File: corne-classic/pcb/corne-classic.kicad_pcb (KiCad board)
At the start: 2 copper layers, 133.8 x 92.2 mm, 98 parts, among them J1 MJ-4PP-9, J2 OLED, J3 LED, P1 i2c-pin, P2 i2c-pin, SW1 SW_PUSH, SW10 SW_PUSH, SW11 SW_PUSH, SW12 SW_PUSH, SW13 SW_PUSH, SW14 SW_PUSH, SW15 SW_PUSH, SW16 SW_PUSH, SW17 SW_PUSH, SW18 SW_PUSH, SW19 SW_PUSH, SW2 SW_PUSH, SW20 SW_PUSH, SW21 SW_PUSH, SW3 SW_PUSH, SW4 SW_PUSH, SW5 SW_PUSH, SW6 SW_PUSH, SW7 SW_PUSH, SW8 SW_PUSH, SW9 SW_PUSH, U1 ProMicro

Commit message: new stuff
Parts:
- removed the ? at (177.8, 115.8)
- removed the ? at (192.2, 124.2)
- removed the ? at (79.5, 86.8)
- removed the ? at (98.5, 86.8)
- removed the ? at (98.5, 105.8)
- removed the ? at (155.5, 83.0)
- removed the ? at (122.8, 122.8)
- removed G*** (x2): LOGO, kbd:corne
- added ?: , kbd:LEGO_HOLE2, F.Cu at (192.2, 124.2)
- added ?: , kbd:LEGO_HOLE, F.Cu at (155.5, 64.0)
- added ?: , kbd:LEGO_HOLE, F.Cu at (103.8, 122.8)
- added ?: , kbd:LEGO_HOLE, F.Cu at (155.5, 101.8)
- added ?: , kbd:LEGO_HOLE, F.Cu at (117.5, 62.0)
- added ?: , kbd:LEGO_HOLE, F.Cu at (79.5, 67.8)
- added ?: , kbd:LEGO_HOLE2, F.Cu at (177.8, 115.8)
- added D22: D, kbd:D3_TH_SMD, F.Cu at (135.0, 108.0)
- added D23: D, kbd:D3_TH_SMD, F.Cu at (154.0, 110.4)
- added D24: D, kbd:D3_TH_SMD, F.Cu at (157.0, 112.8)
- added D25: D, kbd:D3_TH_SMD, F.Cu at (109.5, 130.0)
- added D26: D, kbd:D3_TH_SMD, F.Cu at (125.5, 130.0)
- added D27: D, kbd:D3_TH_SMD, F.Cu at (144.5, 129.8)
- added D28: D, kbd:D3_TH_SMD, F.Cu at (147.5, 129.8)
- added L28: SK6812MINI, kbd:SK6812MINI_rev, F.Cu at (127.0, 102.5)
- added L29: SK6812MINI, kbd:SK6812MINI_rev, F.Cu at (146.0, 104.9)
- added L30: SK6812MINI, kbd:SK6812MINI_rev, F.Cu at (165.0, 107.2)
- added L31: SK6812MINI, kbd:SK6812MINI_rev, F.Cu at (117.5, 124.5)
- added L32: SK6812MINI, kbd:SK6812MINI_rev, F.Cu at (136.5, 124.5)
- added L33: SK6812MINI, kbd:SK6812MINI_rev, F.Cu at (159.0, 127.5)
- added L34: SK6812MINI, kbd:SK6812MINI_rev, F.Cu at (175.0, 133.8)
- added SW22: SW_PUSH, kbd:MX_ALPS_PG1350_noLed, F.Cu at (127.0, 108.0)
- added SW23: SW_PUSH, kbd:MX_ALPS_PG1350_noLed, F.Cu at (146.0, 110.4)
- added SW24: SW_PUSH, kbd:MX_ALPS_PG1350_noLed, F.Cu at (165.0, 112.8)
- added SW25: SW_PUSH, kbd:MX_ALPS_PG1350_noLed, F.Cu at (117.5, 130.0)
- added SW26: SW_PUSH, kbd:MX_ALPS_PG1350_noLed, F.Cu at (136.5, 130.0)
- added SW27: SW_PUSH, kbd:MX_ALPS_PG1350_noLed, F.Cu at (157.5, 132.8)
- added SW28: SW_PUSH, kbd:MX_ALPS_PG1350_noLed_1.75u, F.Cu at (179.8, 136.5)
- SW21: footprint kbd:MX_ALPS_PG1350_noLed_1.75u -> kbd:MX_ALPS_PG1350_noLed
- moved SW21 76.4 mm to (108.0, 110.4), turned to 180 degrees
- moved L27 73.0 mm to (108.0, 104.9), turned to 0 degrees
- moved L26 72.2 mm to (89.0, 109.6), turned to 0 degrees
- moved SW20 70.7 mm to (89.0, 115.1), turned to 180 degrees
- moved D19 68.1 mm to (62.0, 115.1)
- moved L25 68.1 mm to (70.0, 109.6)
- moved SW19 68.1 mm to (70.0, 115.1)
- moved D20 49.7 mm to (97.0, 115.1)
- moved D21 37.0 mm to (116.0, 110.4)
- moved D1 19.0 mm to (62.0, 58.1)
- moved D10 19.0 mm to (135.0, 70.0)
- moved D11 19.0 mm to (154.0, 72.4)
- moved D13 19.0 mm to (62.0, 96.1)
- moved D14 19.0 mm to (97.0, 96.1)
- moved D15 19.0 mm to (116.0, 91.4)
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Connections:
- L19 pad 1: Net-(L13-Pad1) (its old number) -> Net-(L19-Pad1)
- L20 pad 3: Net-(L14-Pad3) (its old number) -> Net-(L20-Pad3)
- L21 pad 1: Net-(L14-Pad3) (its old number) -> Net-(L21-Pad1)
- L22 pad 3: Net-(L16-Pad3) (its old number) -> Net-(L22-Pad3)
- L23 pad 1: Net-(L17-Pad1) (its old number) -> Net-(L23-Pad1)
- L24 pad 3: Net-(L18-Pad3) (its old number) -> Net-(L24-Pad3)
- L25 pad 1: Net-(L16-Pad3) (its old number) -> Net-(L25-Pad1)
- L25 pad 3: Net-(L19-Pad3) -> Net-(L19-Pad1)
- L26 pad 1: Net-(L19-Pad3) -> Net-(L20-Pad3)
- L26 pad 3: Net-(L17-Pad1) (its old number) -> Net-(L26-Pad3)
- L27 pad 1: Net-(L18-Pad3) (its old number) -> Net-(L27-Pad1)
- L27 pad 3: Net-(L21-Pad3) -> Net-(L21-Pad1)
- L6 pad 1: Net-(L21-Pad3) -> Net-(L34-Pad3)
- SW19 pad 1: col3 -> col0
- SW20 pad 1: col4 -> col1
- SW21 pad 1: col5 -> col2
- U1 pad 11: Net-(U1-Pad11) -> row4
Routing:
- net VCC: track 758.8 -> 979.9 mm, vias 33 -> 45
- net GND: track 797.7 -> 991.4 mm, vias 49 -> 48
- net row4: track 0.00 -> 157.7 mm, vias 0 -> 8
- net row3: track 121.8 -> 229.0 mm, vias 3 -> 10
- net col2: track 197.5 -> 264.3 mm
- net Net-(L20-Pad3): track 0.00 -> 55.2 mm, vias 0 -> 6
- net Net-(D28-Pad2): track 0.00 -> 53.7 mm
- net Net-(L29-Pad1): track 0.00 -> 50.8 mm, vias 0 -> 5
- net Net-(L21-Pad1): track 0.00 -> 50.1 mm, vias 0 -> 2
- net col4: track 194.3 -> 244.3 mm, vias 6 -> 8
- net Net-(L17-Pad1) (its old number): track 49.6 -> 0.00 mm, vias 4 -> 0
- net Net-(L27-Pad1): track 0.00 -> 48.8 mm, vias 0 -> 2
- net Net-(L26-Pad3): track 0.00 -> 46.6 mm, vias 0 -> 6
- net Net-(L22-Pad3): track 0.00 -> 46.0 mm, vias 0 -> 4
- net Net-(L23-Pad1): track 0.00 -> 45.9 mm, vias 0 -> 4
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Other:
- board size 133.8 x 92.2 mm -> 133.8 x 111.2 mm
- board text removed: "Corne Classic v2.0 PCB Designed by foostan"
- board text removed: "GND"
- board text removed: "LED"
- board text removed: "OLED"
- board text removed: "VCC"

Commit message: fixed some connections
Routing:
- net row3: track 229.0 -> 224.5 mm, vias 10 -> 9
- net row2: track 213.5 -> 210.6 mm, vias 10 -> 9
- net col0: track 285.9 -> 283.6 mm
- net row1: track 198.3 -> 197.1 mm
- net row0: track 203.9 -> 203.1 mm

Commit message: further routing fixes
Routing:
- net GND: track 991.4 -> 984.5 mm
- net VCC: track 979.9 -> 975.8 mm
- net Net-(L30-Pad3): track 39.7 -> 38.3 mm
- net col5: track 215.2 -> 213.9 mm
- net row2: track 210.6 -> 209.5 mm, vias 9 -> 8
- net LED: track 71.9 -> 70.9 mm
- net Net-(L10-Pad1): track 20.9 -> 20.0 mm
- net row4: track 157.7 -> 156.9 mm
- net Net-(L7-Pad3): track 21.5 -> 22.3 mm
- net Net-(L19-Pad1): track 38.3 -> 37.6 mm
- net Net-(L12-Pad3): track 39.1 -> 38.6 mm

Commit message: routing
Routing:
- net Net-(D27-Pad2): track 23.2 -> 19.3 mm
- net col0: track 283.7 -> 280.9 mm
- net VCC: track 975.8 -> 978.2 mm
- net Net-(L4-Pad1): track 74.1 -> 71.9 mm
- net col1: track 254.4 -> 253.1 mm
- net Net-(L29-Pad1): track 50.8 -> 51.9 mm
- net col4: track 243.9 -> 242.9 mm
- net GND: track 984.5 -> 983.7 mm
- net Net-(D28-Pad2): track 53.7 -> 53.0 mm
- net Net-(L13-Pad3): track 38.6 -> 38.0 mm
- net Net-(L26-Pad3): track 46.6 -> 46.1 mm

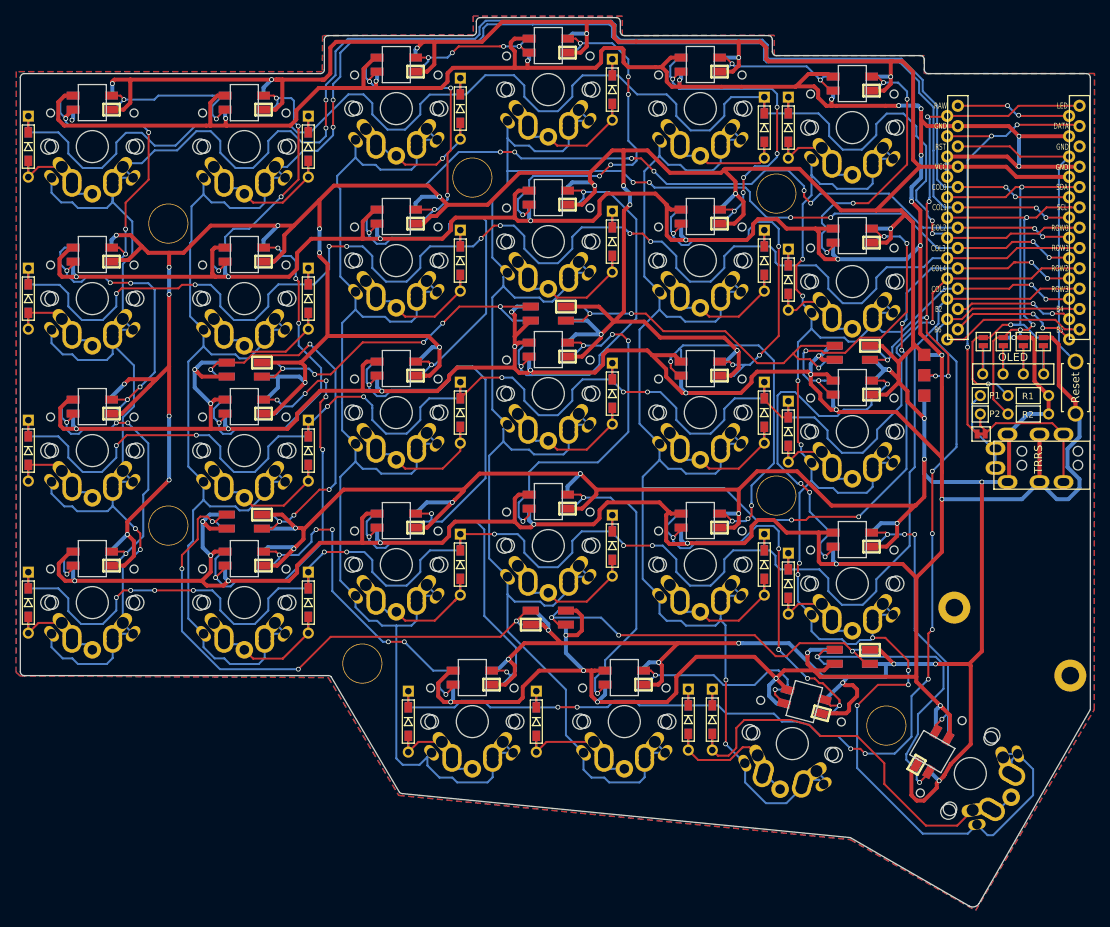
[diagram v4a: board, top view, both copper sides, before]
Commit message: started to change the footprint to fit mill max inside
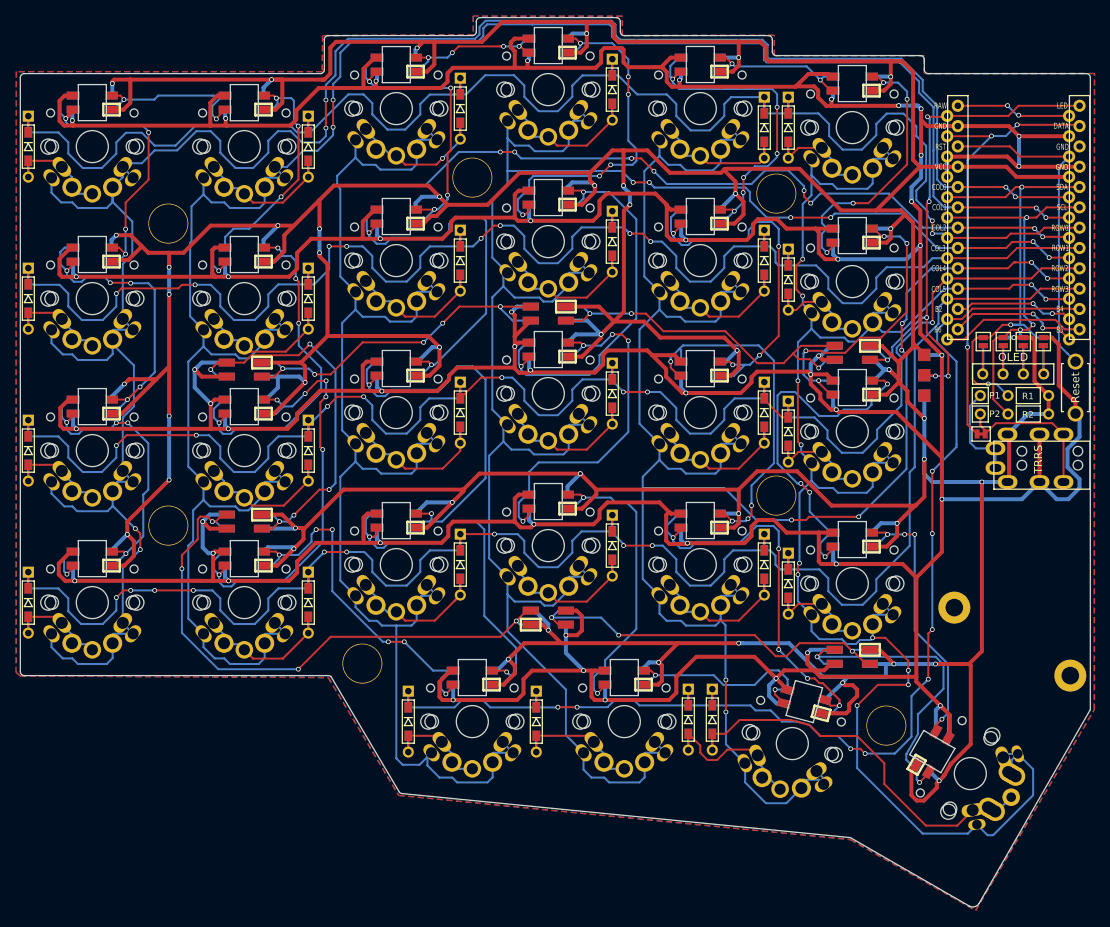
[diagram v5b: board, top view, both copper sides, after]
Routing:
- net Net-(D28-Pad2): track 53.0 -> 50.1 mm
- net Net-(D1-Pad2): track 13.7 -> 15.1 mm
- net Net-(J1-PadA): track 10.9 -> 12.3 mm
- net GND: track 983.7 -> 982.5 mm
- net Net-(D27-Pad2): track 19.3 -> 20.4 mm
- net Net-(L27-Pad1): track 48.8 -> 49.4 mm

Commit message: rerouting
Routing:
- net col2: track 265.0 -> 254.1 mm
- net GND: track 982.5 -> 979.6 mm
- net VCC: track 978.0 -> 976.4 mm
- net col5: track 213.6 -> 212.5 mm
- net Net-(D28-Pad2): track 50.1 -> 49.0 mm
- net Net-(L27-Pad1): track 49.4 -> 48.7 mm
- net Net-(L23-Pad1): track 46.1 -> 46.7 mm

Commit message: added text
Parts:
- moved ? 10.0 mm to (192.2, 114.2)
- moved ? 10.0 mm to (177.8, 105.8)
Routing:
- net GND: track 979.6 -> 980.2 mm, vias 48 -> 157
- net (no net): vias 0 -> 4
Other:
- board text added: "corne-ext designed by XWaVeX"
